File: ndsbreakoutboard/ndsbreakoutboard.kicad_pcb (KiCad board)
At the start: 2 copper layers, 2 parts, among them J1 Conn_01x17_Female, U1 ndsPADS

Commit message: Commit before rebuilding netlist with pin headers
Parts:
- removed J1: Conn_01x17_Female, Connector_PinHeader_2.54mm:PinHeader_1x17_P2.54mm_Vertical
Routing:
- net (no net): vias 0 -> 19
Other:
- board outline added: 27.3 x 30.5 mm
- board text added: "3.3V"
- board text added: "?"
- board text added: "CLK"
- board text added: "CS1"
- board text added: "CS2"
- board text added: "D0"
- board text added: "D1"
- board text added: "D2"
- board text added: "D3"
- board text added: "D4"
- board text added: "D5"
- board text added: "D6"
- board text added: "D7"
- board text added: "GND"
- board text added: "IRQ"
- board text added: "Nintendo DS & 3DS Breakout Board github.com/pedro-javierf/dscartpcb"
- board text added: "RES"
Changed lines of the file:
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@@
   (general
     (thickness 1.6)
-    (drawings 0)
-    (tracks 0)
+    (drawings 26)
+    (tracks 19)
     (zones 0)
-    (modules 2)
+    (modules 1)
     (nets 18)
   )
@@
     (47 F.CrtYd user)
     (48 B.Fab user)
-    (49 F.Fab user)
+    (49 F.Fab user hide)
   )
   (setup
@@
     (mod_text_size 1 1)
     (mod_text_width 0.15)
-    (pad_size 1.524 1.524)
-    (pad_drill 0.762)
+    (pad_size 0.85 0.85)
+    (pad_drill 0)
     (pad_to_mask_clearance 0.051)
     (solder_mask_min_width 0.25)
@@
     (add_net "Net-(J1-Pad9)")
   )
-  (module Connector_PinHeader_2.54mm:PinHeader_1x17_P2.54mm_Vertical (layer F.Cu)
-    (at 77.47 69.85 90)
-    (descr "Through hole straight pin header, 1x17, 2.54mm pitch, single row")
-    (tags "Through hole pin header THT 1x17 2.54mm single row")
-    (fp_text reference J1 (at 0 -2.33 90) (layer F.SilkS)
-      (effects (font (size 1 1) (thickness 0.15)))
-    )
-    (fp_text value Conn_01x17_Female (at 0 42.97 90) (layer F.Fab)
-      (effects (font (size 1 1) (thickness 0.15)))
-    )
-    (fp_line (start -0.635 -1.27) (end 1.27 -1.27) (layer F.Fab) (width 0.1))
-    (fp_line (start 1.27 -1.27) (end 1.27 41.91) (layer F.Fab) (width 0.1))
-    (fp_line (start 1.27 41.91) (end -1.27 41.91) (layer F.Fab) (width 0.1))
-    (fp_line (start -1.27 41.91) (end -1.27 -0.635) (layer F.Fab) (width 0.1))
-    (fp_line (start -1.27 -0.635) (end -0.635 -1.27) (layer F.Fab) (width 0.1))
-    (fp_line (start -1.33 41.97) (end 1.33 41.97) (layer F.SilkS) (width 0.12))
-    (fp_line (start -1.33 1.27) (end -1.33 41.97) (layer F.SilkS) (width 0.12))
-    (fp_line (start 1.33 1.27) (end 1.33 41.97) (layer F.SilkS) (width 0.12))
-    (fp_line (start -1.33 1.27) (end 1.33 1.27) (layer F.SilkS) (width 0.12))
-    (fp_line (start -1.33 0) (end -1.33 -1.33) (layer F.SilkS) (width 0.12))
-    (fp_line (start -1.33 -1.33) (end 0 -1.33) (layer F.SilkS) (width 0.12))
-    (fp_line (start -1.8 -1.8) (end -1.8 42.45) (layer F.CrtYd) (width 0.05))
-    (fp_line (start -1.8 42.45) (end 1.8 42.45) (layer F.CrtYd) (width 0.05))
-    (fp_line (start 1.8 42.45) (end 1.8 -1.8) (layer F.CrtYd) (width 0.05))
-    (fp_line (start 1.8 -1.8) (end -1.8 -1.8) (layer F.CrtYd) (width 0.05))
-    (fp_text user %R (at 0 20.32) (layer F.Fab)
-      (effects (font (size 1 1) (thickness 0.15)))
-    )
-    (pad 1 thru_hole rect (at 0 0 90) (size 1.7 1.7) (drill 1) (layers *.Cu *.Mask)
-      (net 1 "Net-(J1-Pad1)"))
-    (pad 2 thru_hole oval (at 0 2.54 90) (size 1.7 1.7) (drill 1) (layers *.Cu *.Mask)
-      (net 2 "Net-(J1-Pad2)"))
-    (pad 3 thru_hole oval (at 0 5.08 90) (size 1.7 1.7) (drill 1) (layers *.Cu *.Mask)
-      (net 3 "Net-(J1-Pad3)"))
-    (pad 4 thru_hole oval (at 0 7.62 90) (size 1.7 1.7) (drill 1) (layers *.Cu *.Mask)
-      (net 4 "Net-(J1-Pad4)"))
-    (pad 5 thru_hole oval (at 0 10.16 90) (size 1.7 1.7) (drill 1) (layers *.Cu *.Mask)
-      (net 5 "Net-(J1-Pad5)"))
-    (pad 6 thru_hole oval (at 0 12.7 90) (size 1.7 1.7) (drill 1) (layers *.Cu *.Mask)
-      (net 6 "Net-(J1-Pad6)"))
-    (pad 7 thru_hole oval (at 0 15.24 90) (size 1.7 1.7) (drill 1) (layers *.Cu *.Mask)
-      (net 7 "Net-(J1-Pad7)"))
-    (pad 8 thru_hole oval (at 0 17.78 90) (size 1.7 1.7) (drill 1) (layers *.Cu *.Mask)
-      (net 8 "Net-(J1-Pad8)"))
-    (pad 9 thru_hole oval (at 0 20.32 90) (size 1.7 1.7) (drill 1) (layers *.Cu *.Mask)
-      (net 9 "Net-(J1-Pad9)"))
-    (pad 10 thru_hole oval (at 0 22.86 90) (size 1.7 1.7) (drill 1) (layers *.Cu *.Mask)
-      (net 10 "Net-(J1-Pad10)"))
-    (pad 11 thru_hole oval (at 0 25.4 90) (size 1.7 1.7) (drill 1) (layers *.Cu *.Mask)
-      (net 11 "Net-(J1-Pad11)"))
-    (pad 12 thru_hole oval (at 0 27.94 90) (size 1.7 1.7) (drill 1) (layers *.Cu *.Mask)
-      (net 12 "Net-(J1-Pad12)"))
-    (pad 13 thru_hole oval (at 0 30.48 90) (size 1.7 1.7) (drill 1) (layers *.Cu *.Mask)
-      (net 13 "Net-(J1-Pad13)"))
-    (pad 14 thru_hole oval (at 0 33.02 90) (size 1.7 1.7) (drill 1) (layers *.Cu *.Mask)
-      (net 14 "Net-(J1-Pad14)"))
-    (pad 15 thru_hole oval (at 0 35.56 90) (size 1.7 1.7) (drill 1) (layers *.Cu *.Mask)
-      (net 15 "Net-(J1-Pad15)"))
-    (pad 16 thru_hole oval (at 0 38.1 90) (size 1.7 1.7) (drill 1) (layers *.Cu *.Mask)
-      (net 16 "Net-(J1-Pad16)"))
-    (pad 17 thru_hole oval (at 0 40.64 90) (size 1.7 1.7) (drill 1) (layers *.Cu *.Mask)
-      (net 17 "Net-(J1-Pad17)"))
-    (model ${KISYS3DMOD}/Connector_PinHeader_2.54mm.3dshapes/PinHeader_1x17_P2.54mm_Vertical.wrl
-      (at (xyz 0 0 0))
-      (scale (xyz 1 1 1))
-      (rotate (xyz 0 0 0))
-    )
-  )
   (module Connector:nds_contact_pads (layer F.Cu)
     (at 92.770001 84.705)
     (descr "A footprint for the bottom pads of the NDS cartridge")
     (tags "nds nintendo ds 3ds dsi pads bottom cart card")
-    (fp_text reference U1 (at 0 20.32) (layer F.SilkS)
-      (effects (font (size 1 1) (thickness 0.15)))
+    (fp_text reference U1 (at 0.143199 -4.0854) (layer F.SilkS)
+      (effects (font (size 0.8 0.8) (thickness 0.15)))
     )
-    (fp_text value ndsPADS (at 0 -0.5) (layer F.Fab)
+    (fp_text value ndsPADS (at 5.019999 -5.33) (layer F.Fab)
       (effects (font (size 1 1) (thickness 0.15)))
     )
@@
       (net 17 "Net-(J1-Pad17)"))
   )
+  (gr_text "Nintendo DS & 3DS Breakout Board\ngithub.com/pedro-javierf/dscartpcb" (at 98.075 72.95) (layer B.Cu)
+    (effects (font (size 0.9 0.9) (thickness 0.15)) (justify mirror))
+  )
+  (gr_line (start 84.455 80.9498) (end 84.45 92.075) (layer Edge.Cuts) (width 0.12))
+  (gr_arc (start 84.475 79.725) (end 84.455 80.9498) (angle -181.8343179) (layer Edge.Cuts) (width 0.12))
+  (gr_line (start 111.76 78.486) (end 111.76 61.595) (layer Edge.Cuts) (width 0.12))
+  (gr_arc (start 111.75 79.75) (end 111.76 78.486) (angle -180.9026615) (layer Edge.Cuts) (width 0.12))
+  (gr_text D7 (at 108.25 84.225 90) (layer F.SilkS)
+    (effects (font (size 1 1) (thickness 0.15)))
+  )
+  (gr_text D6 (at 106.75 84.225 90) (layer F.SilkS)
+    (effects (font (size 1 1) (thickness 0.15)))
+  )
+  (gr_text D5 (at 105.175 84.225 90) (layer F.SilkS)
+    (effects (font (size 1 1) (thickness 0.15)))
+  )
+  (gr_text D4 (at 103.7 84.225 90) (layer F.SilkS)
+    (effects (font (size 1 1) (thickness 0.15)))
+  )
+  (gr_text D3 (at 102.2 84.25 90) (layer F.SilkS)
+    (effects (font (size 1 1) (thickness 0.15)))
+  )
+  (gr_text D2 (at 100.675 84.275 90) (layer F.SilkS)
+    (effects (font (size 1 1) (thickness 0.15)))
+  )
+  (gr_text D1 (at 99.15 84.275 90) (layer F.SilkS)
+    (effects (font (size 1 1) (thickness 0.15)))
+  )
+  (gr_text D0 (at 97.7 84.3 90) (layer F.SilkS)
+    (effects (font (size 1 1) (thickness 0.15)))
+  )
+  (gr_text 3.3V (at 96.25 83.55 90) (layer F.SilkS)
+    (effects (font (size 1 1) (thickness 0.15)))
+  )
+  (gr_text IRQ (at 94.675 84 90) (layer F.SilkS)
+    (effects (font (size 1 1) (thickness 0.15)))
+  )
+  (gr_text CS2 (at 93.2 83.775 90) (layer F.SilkS)
+    (effects (font (size 1 1) (thickness 0.15)))
+  )
+  (gr_text RES (at 91.725 83.775 90) (layer F.SilkS)
+    (effects (font (size 1 1) (thickness 0.15)))
+  )
+  (gr_text CS1 (at 90.175 83.775 90) (layer F.SilkS)
+    (effects (font (size 1 1) (thickness 0.15)))
+  )
+  (gr_text ? (at 88.646 83.82) (layer F.SilkS)
+    (effects (font (size 1 1) (thickness 0.15)))
+  )
+  (gr_text CLK (at 87.25 83.85 90) (layer F.SilkS)
+    (effects (font (size 1 1) (thickness 0.15)))
+  )
+  (gr_text GND (at 109.775 83.7565 90) (layer F.SilkS)
+    (effects (font (size 1 1) (thickness 0.15)))
+  )
+  (gr_text GND (at 85.725 83.75 90) (layer F.SilkS)
+    (effects (font (size 1 1) (thickness 0.15)))
+  )
+  (gr_line (start 84.455 61.595) (end 84.455785 78.500187) (layer Edge.Cuts) (width 0.12))
+  (gr_line (start 111.76 61.595) (end 84.455 61.595) (layer Edge.Cuts) (width 0.12))
+  (gr_line (start 111.76 92.075) (end 111.759914 81.014001) (layer Edge.Cuts) (width 0.12))
+  (gr_line (start 84.45 92.075) (end 111.76 92.075) (layer Edge.Cuts) (width 0.12))
+  (via (at 85.6615 81.788) (size 0.8) (drill 0.4) (layers F.Cu B.Cu) (net 0))
+  (via (at 87.1855 81.788) (size 0.8) (drill 0.4) (layers F.Cu B.Cu) (net 0))
+  (via (at 88.7095 81.788) (size 0.8) (drill 0.4) (layers F.Cu B.Cu) (net 0))
+  (via (at 90.17 81.788) (size 0.8) (drill 0.4) (layers F.Cu B.Cu) (net 0))
+  (via (at 91.6305 81.788) (size 0.8) (drill 0.4) (layers F.Cu B.Cu) (net 0))
+  (via (at 93.091 81.788) (size 0.8) (drill 0.4) (layers F.Cu B.Cu) (net 0))
+  (via (at 94.5515 81.788) (size 0.8) (drill 0.4) (layers F.Cu B.Cu) (net 0))
+  (via (at 96.139 81.28) (size 0.8) (drill 0.4) (layers F.Cu B.Cu) (net 0))
+  (via (at 97.5995 81.788) (size 0.8) (drill 0.4) (layers F.Cu B.Cu) (net 0))
+  (via (at 99.06 81.788) (size 0.8) (drill 0.4) (layers F.Cu B.Cu) (net 0))
+  (via (at 100.6475 81.788) (size 0.8) (drill 0.4) (layers F.Cu B.Cu) (net 0))
+  (via (at 102.108 81.788) (size 0.8) (drill 0.4) (layers F.Cu B.Cu) (net 0))
+  (via (at 103.632 81.788) (size 0.8) (drill 0.4) (layers F.Cu B.Cu) (net 0))
+  (via (at 105.156 81.788) (size 0.8) (drill 0.4) (layers F.Cu B.Cu) (net 0))
+  (via (at 106.6165 81.788) (size 0.8) (drill 0.4) (layers F.Cu B.Cu) (net 0))
+  (via (at 108.1405 81.788) (size 0.8) (drill 0.4) (layers F.Cu B.Cu) (net 0))
+  (via (at 109.728 81.788) (size 0.8) (drill 0.4) (layers F.Cu B.Cu) (net 0))
+  (via (at 107.65 66.025) (size 2.1) (drill 2) (layers F.Cu B.Cu) (net 0))
+  (via (at 88.8 66.025) (size 2.1) (drill 2) (layers F.Cu B.Cu) (net 0))
 )

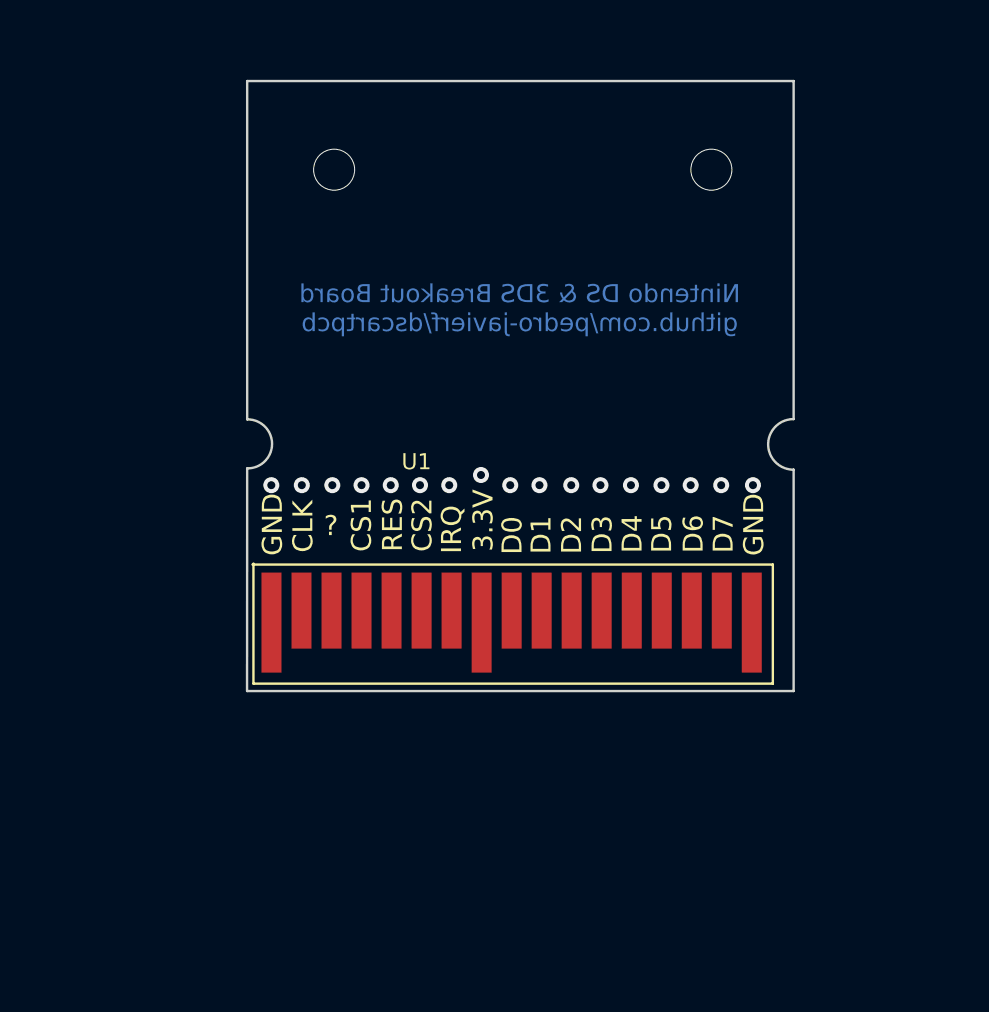
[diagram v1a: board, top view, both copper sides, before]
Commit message: Final iteration finished
- correct eschematics
- pcb design finished
- pcb improvements
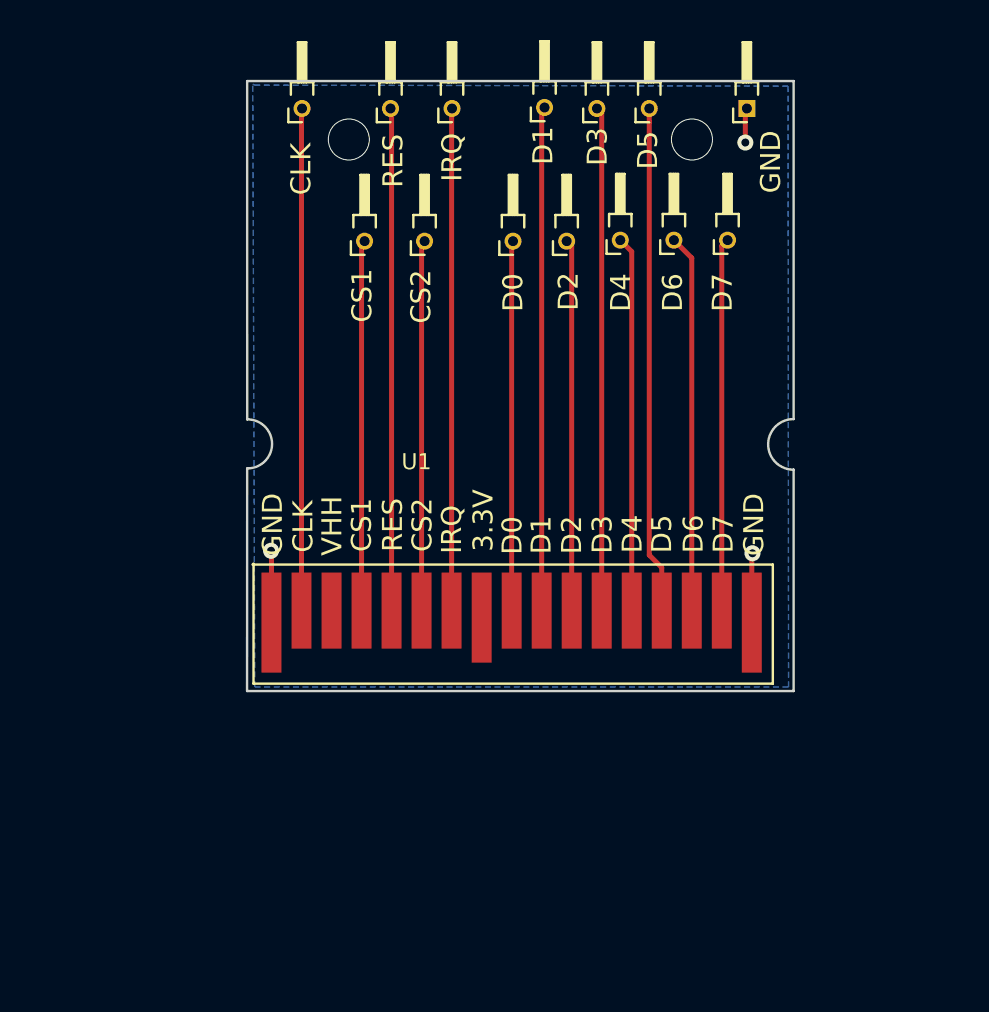
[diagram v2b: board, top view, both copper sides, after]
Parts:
- added CLK: Conn_01x01_Female, Connector_PinHeader_1.00mm:PinHeader_1x01_P1.00mm_Horizontal, F.Cu at (87.2, 63.0)
- added CS1: Conn_01x01_Female, Connector_PinHeader_1.00mm:PinHeader_1x01_P1.00mm_Horizontal, F.Cu at (90.3, 69.6)
- added CS2: Conn_01x01_Female, Connector_PinHeader_1.00mm:PinHeader_1x01_P1.00mm_Horizontal, F.Cu at (93.3, 69.6)
- added D0: Conn_01x01_Female, Connector_PinHeader_1.00mm:PinHeader_1x01_P1.00mm_Horizontal, F.Cu at (97.7, 69.6)
- added D1: Conn_01x01_Female, Connector_PinHeader_1.00mm:PinHeader_1x01_P1.00mm_Horizontal, F.Cu at (99.3, 62.9)
- added D2: Conn_01x01_Female, Connector_PinHeader_1.00mm:PinHeader_1x01_P1.00mm_Horizontal, F.Cu at (100.4, 69.6)
- added D3: Conn_01x01_Female, Connector_PinHeader_1.00mm:PinHeader_1x01_P1.00mm_Horizontal, F.Cu at (101.9, 63.0)
- added D4: Conn_01x01_Female, Connector_PinHeader_1.00mm:PinHeader_1x01_P1.00mm_Horizontal, F.Cu at (103.1, 69.5)
- added D5: Conn_01x01_Female, Connector_PinHeader_1.00mm:PinHeader_1x01_P1.00mm_Horizontal, F.Cu at (104.5, 63.0)
- added D6: Conn_01x01_Female, Connector_PinHeader_1.00mm:PinHeader_1x01_P1.00mm_Horizontal, F.Cu at (105.8, 69.5)
- added D7: Conn_01x01_Female, Connector_PinHeader_1.00mm:PinHeader_1x01_P1.00mm_Horizontal, F.Cu at (108.5, 69.5)
- added G***: LOGO, Connector:ndsIcon, F.Cu at (103.4, 86.1)
- added G***: LOGO, Connector:3dsIcon, F.Cu at (92.3, 86.2)
- added GND: Conn_01x01_Female, Connector_PinHeader_1.00mm:PinHeader_1x01_P1.00mm_Horizontal, F.Cu at (109.4, 63.0)
- added IRQ: Conn_01x01_Female, Connector_PinHeader_1.00mm:PinHeader_1x01_P1.00mm_Horizontal, F.Cu at (94.7, 63.0)
- added RES: Conn_01x01_Female, Connector_PinHeader_1.00mm:PinHeader_1x01_P1.00mm_Horizontal, F.Cu at (91.6, 63.0)
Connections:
- U1 pad 1: Net-(J1-Pad1) (its old number) -> Net-(GNDLine1-Pad1)
- U1 pad 17: Net-(J1-Pad17) -> Net-(GNDLine1-Pad1)
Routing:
- net Net-(J11-Pad1): track 0.00 -> 25.3 mm
- net Net-(J7-Pad1): track 0.00 -> 25.2 mm
- net Net-(J9-Pad1): track 0.00 -> 25.2 mm
- net Net-(J1-Pad1): track 0.00 -> 25.1 mm
- net Net-(J3-Pad1): track 0.00 -> 25.1 mm
- net Net-(J5-Pad1): track 0.00 -> 25.1 mm
- net Net-(J2-Pad1): track 0.00 -> 20.7 mm
- net Net-(J12-Pad1): track 0.00 -> 18.9 mm
- net Net-(J10-Pad1): track 0.00 -> 18.7 mm
- net Net-(J13-Pad1): track 0.00 -> 18.6 mm
- net Net-(J8-Pad1): track 0.00 -> 18.6 mm
- net Net-(J4-Pad1): track 0.00 -> 18.5 mm
- net Net-(J6-Pad1): track 0.00 -> 18.5 mm
- net Net-(GNDLine1-Pad1): track 0.00 -> 11.2 mm, vias 0 -> 3
- net (no net): vias 19 -> 2
- added copper zone on B.Cu, net Net-(GNDLine1-Pad1)
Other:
- net class Default: clearance 0.2 -> 0.1999
- rule trace_clearance: 0.2 -> 0.1999
- board text added: "VHH"
- board text added: "v1.0"
- board text removed: "?"

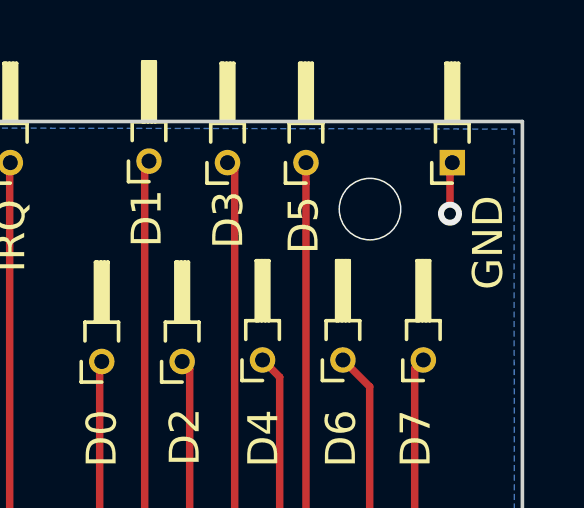
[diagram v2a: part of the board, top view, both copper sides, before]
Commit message: Correct leftover via
Via can be removed
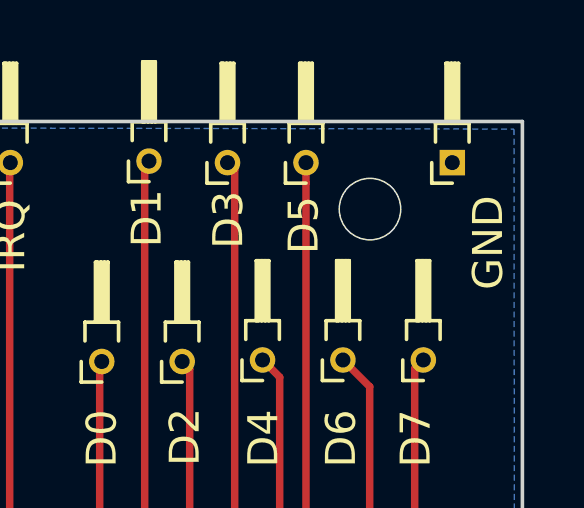
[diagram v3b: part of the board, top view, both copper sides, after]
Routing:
- net Net-(GNDLine1-Pad1): track 11.2 -> 9.53 mm, vias 3 -> 2
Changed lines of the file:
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@@
     (thickness 1.6)
     (drawings 27)
-    (tracks 43)
+    (tracks 41)
     (zones 0)
     (modules 17)
@@
   (via (at 85.6488 85.0646) (size 0.8) (drill 0.4) (layers F.Cu B.Cu) (net 1))
   (via (at 109.7026 85.1916) (size 0.8) (drill 0.4) (layers F.Cu B.Cu) (net 1))
-  (via (at 109.347 64.6684) (size 0.8) (drill 0.4) (layers F.Cu B.Cu) (net 1))
   (segment (start 109.670001 85.224199) (end 109.7026 85.1916) (width 0.25) (layer F.Cu) (net 1))
   (segment (start 109.670001 88.655) (end 109.670001 85.224199) (width 0.25) (layer F.Cu) (net 1))
   (segment (start 109.347 63.0428) (end 109.4232 62.9666) (width 0.25) (layer F.Cu) (net 1))
-  (segment (start 109.347 64.6684) (end 109.347 63.0428) (width 0.25) (layer F.Cu) (net 1))
   (segment (start 85.670001 85.085801) (end 85.6488 85.0646) (width 0.25) (layer F.Cu) (net 1))
   (segment (start 85.670001 88.655) (end 85.670001 85.085801) (width 0.25) (layer F.Cu) (net 1))
